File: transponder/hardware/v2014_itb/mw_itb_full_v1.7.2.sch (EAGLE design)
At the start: 36 parts, among them SW1 SWITCH_SPST-KMT0, SW2 SWITCH_SPST-KMT0

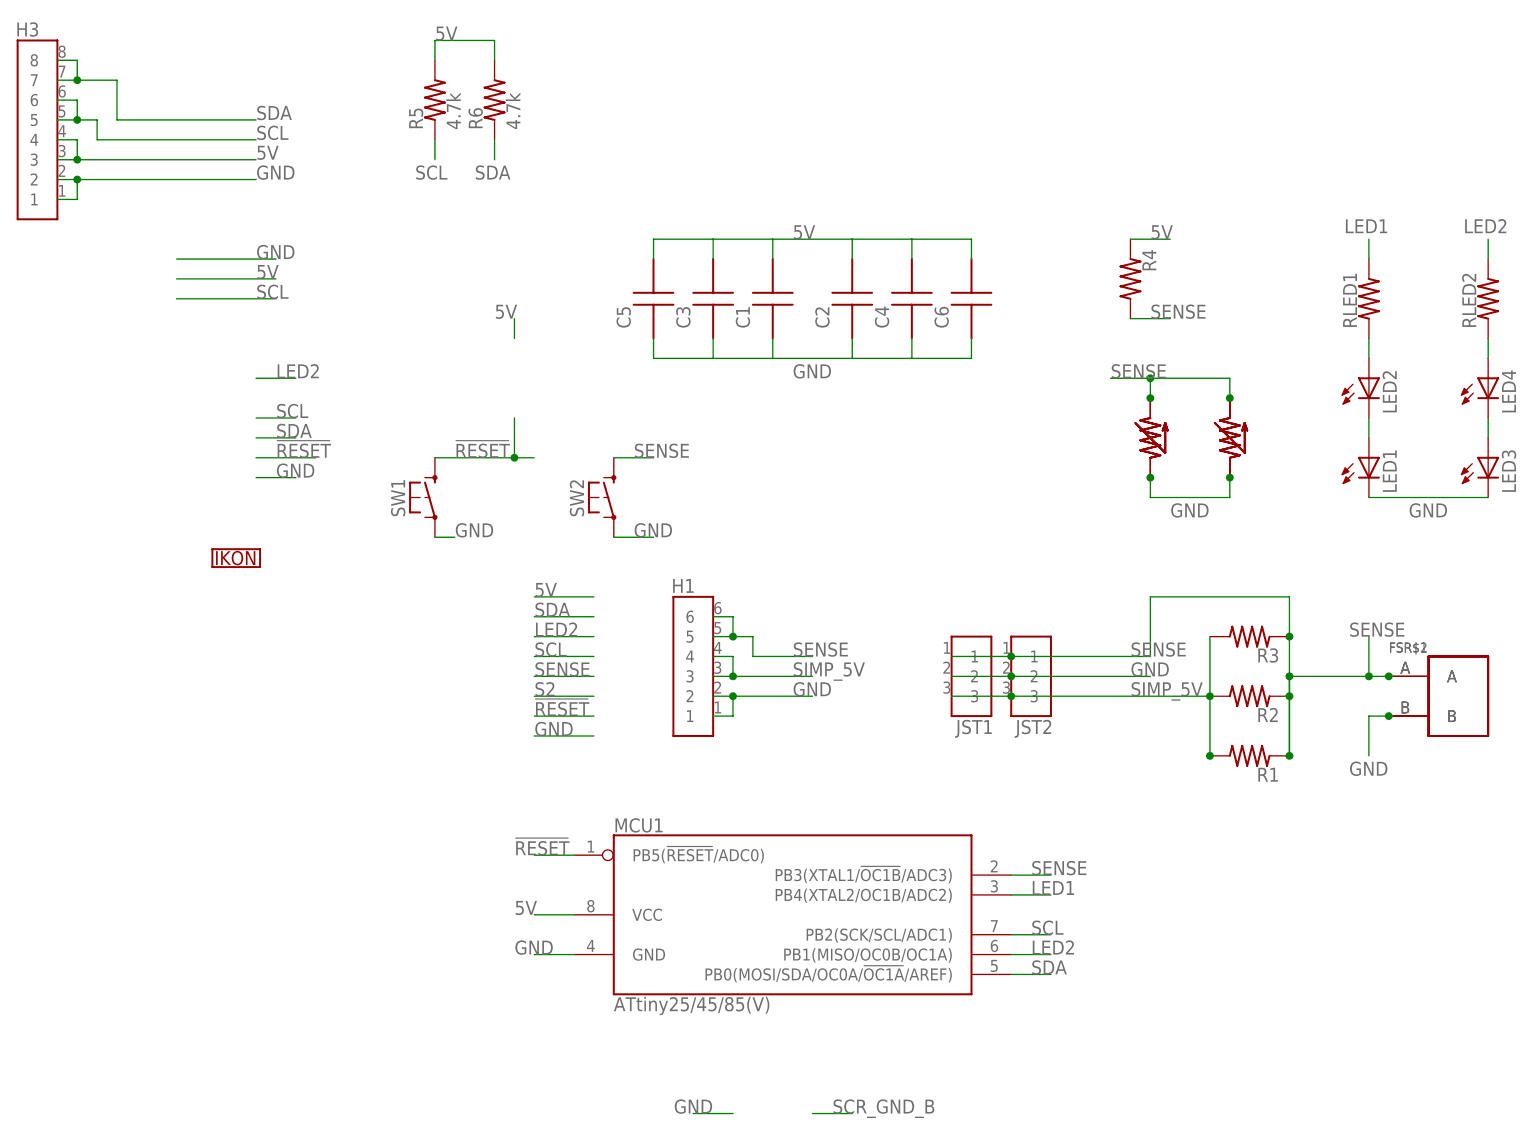
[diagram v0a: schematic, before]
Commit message: Small updates to mw_itb design files.  Basically changed silkscreen for LEDs and added additional button footprint for slightly larger and significantly less expensive TL3315 pushbuttons from E-Switch.   Silkscreen of C&K Components KMT0 footprint was slightly modified to permit it being nested inside new switch footprint.
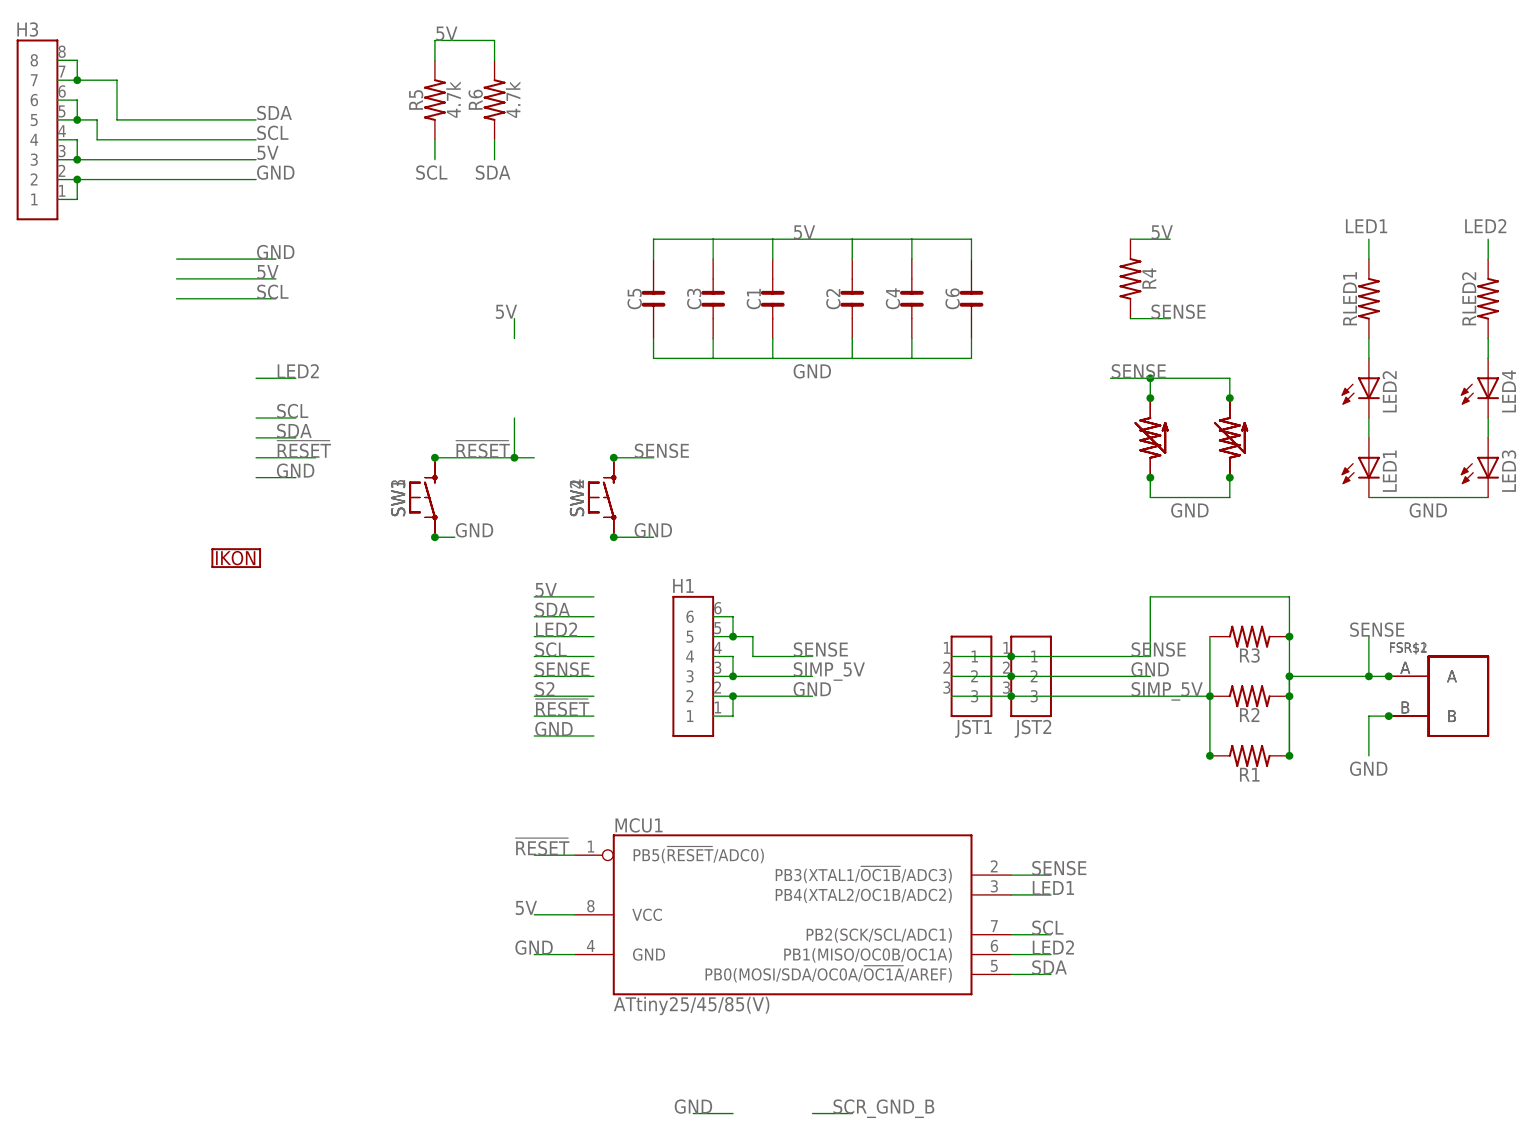
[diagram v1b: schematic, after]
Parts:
- added SW3, SW4: SWITCH_SPST-TL3315, NaN:SWITCH_SPST-TL3315
- C1, C2: device NaN:CAPACITOR1206 -> NaN:CAPACITOR-1206
- C3, C4: device NaN:CAPACITOR0805 -> NaN:CAPACITOR-0805
- C5, C6: device NaN:CAPACITOR0603 -> NaN:CAPACITOR-0603
- R1: device NaN:RESISTOR1206 -> NaN:RESISTOR-1206
- R2: device NaN:RESISTOR0805 -> NaN:RESISTOR-0805
- R3, R4, R5, R6, RLED1, RLED2: device NaN:RESISTOR0603 -> NaN:RESISTOR-0603
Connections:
- net !RESET: now also SW3.1
- net 5V: now also C1.P$2, C2.P$2, C3.P$2, C4.P$2, C5.P$2, C6.P$2; no longer C1.P$1, C2.P$1, C3.P$1, C4.P$1, C5.P$1, C6.P$1
- net GND: now also C1.P$1, C2.P$1, C3.P$1, C4.P$1, C5.P$1, C6.P$1, SW3.2, SW4.2; no longer C1.P$2, C2.P$2, C3.P$2, C4.P$2, C5.P$2, C6.P$2
- net SENSE: now also SW4.1
